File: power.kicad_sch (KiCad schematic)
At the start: 37 parts, among them IC1 MP2456GJ-Z, IC2 MP2456GJ-Z, U4 AP2112K-3.3TRG1, U5 AP2112K-1.8TRG1

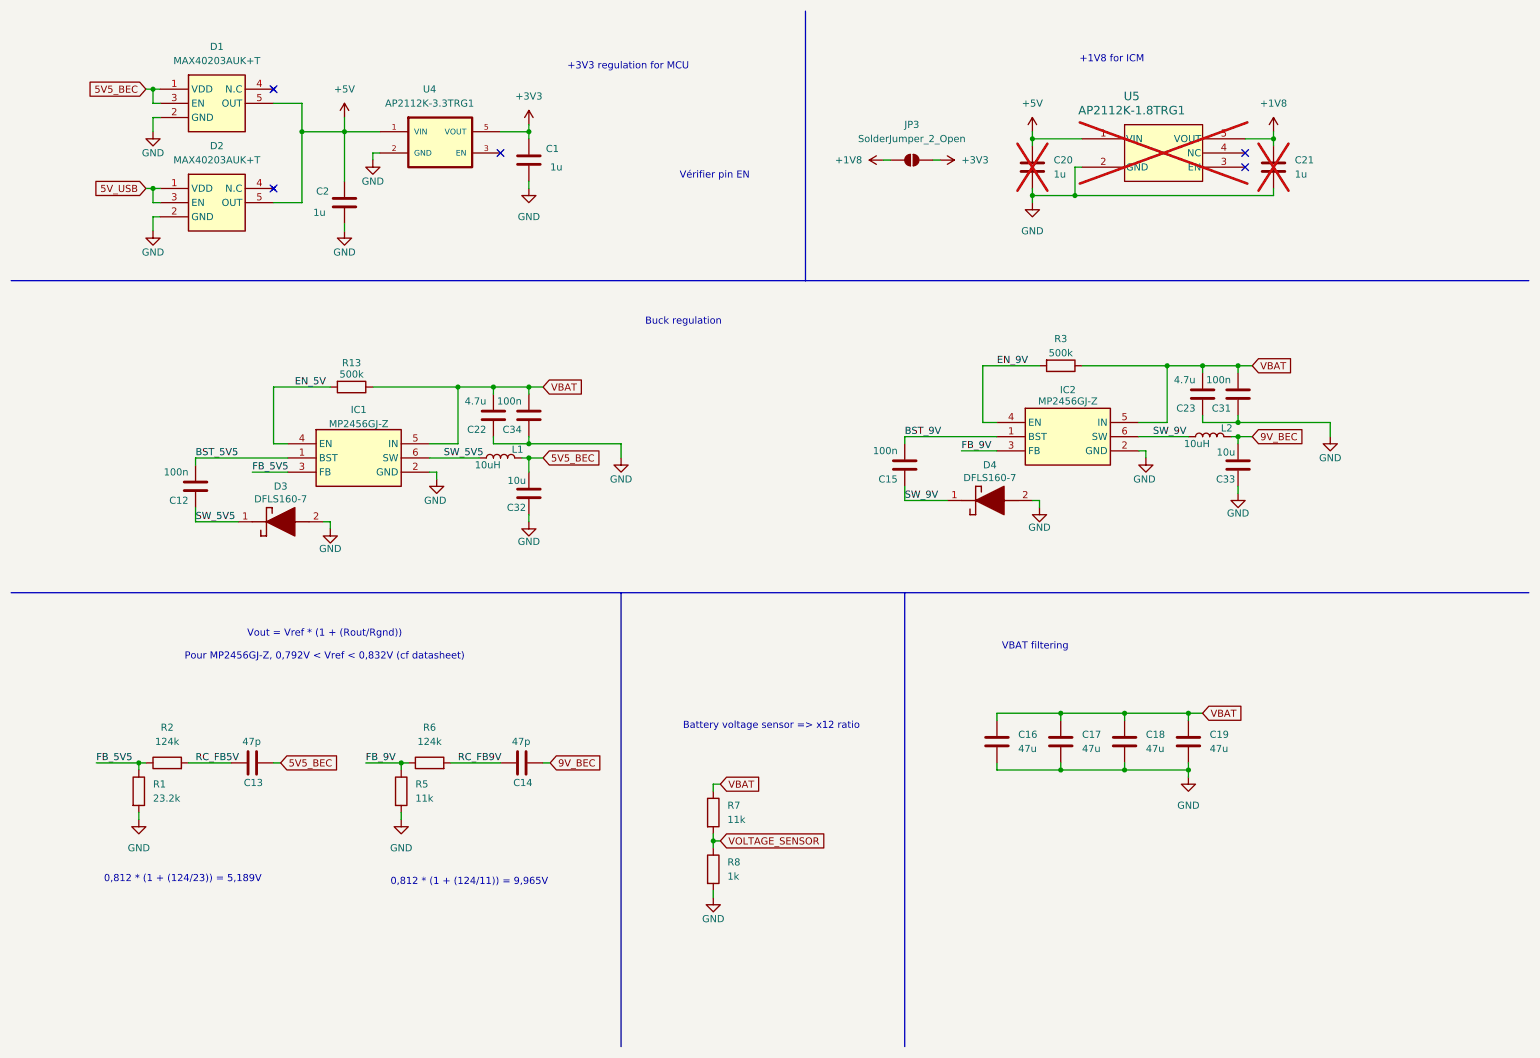
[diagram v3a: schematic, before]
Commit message: add microsd card connector
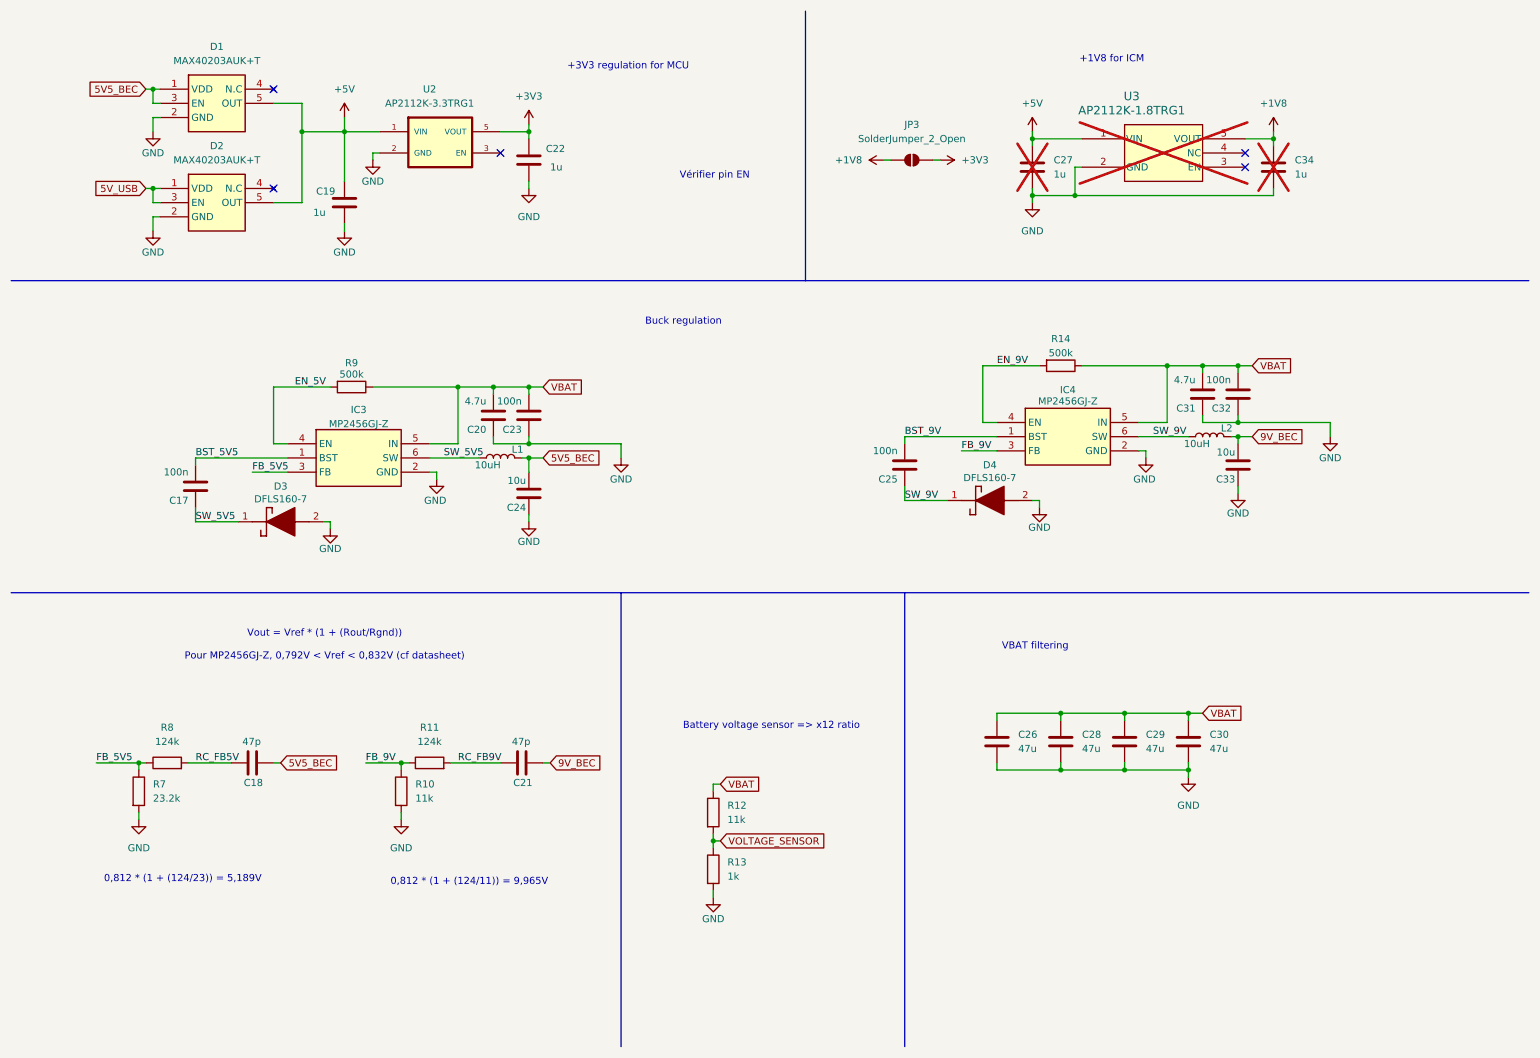
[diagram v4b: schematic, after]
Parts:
- renumbered C12 to C17, C13 to C18, C2 to C19, C22 to C20, C14 to C21, C1 to C22, C34 to C23, C32 to C24, C15 to C25, C16 to C26, C20 to C27, C17 to C28, C18 to C29, C19 to C30, C23 to C31, C31 to C32, C21 to C34, IC1 to IC3, IC2 to IC4, R5 to R10, R6 to R11, R7 to R12, R8 to R13, R3 to R14, R1 to R7, R2 to R8, R13 to R9, U4 to U2, U5 to U3
